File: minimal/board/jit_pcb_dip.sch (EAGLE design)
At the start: 44 parts, among them Q2 MC-306 32.7680K-A0, U1 FT232RL

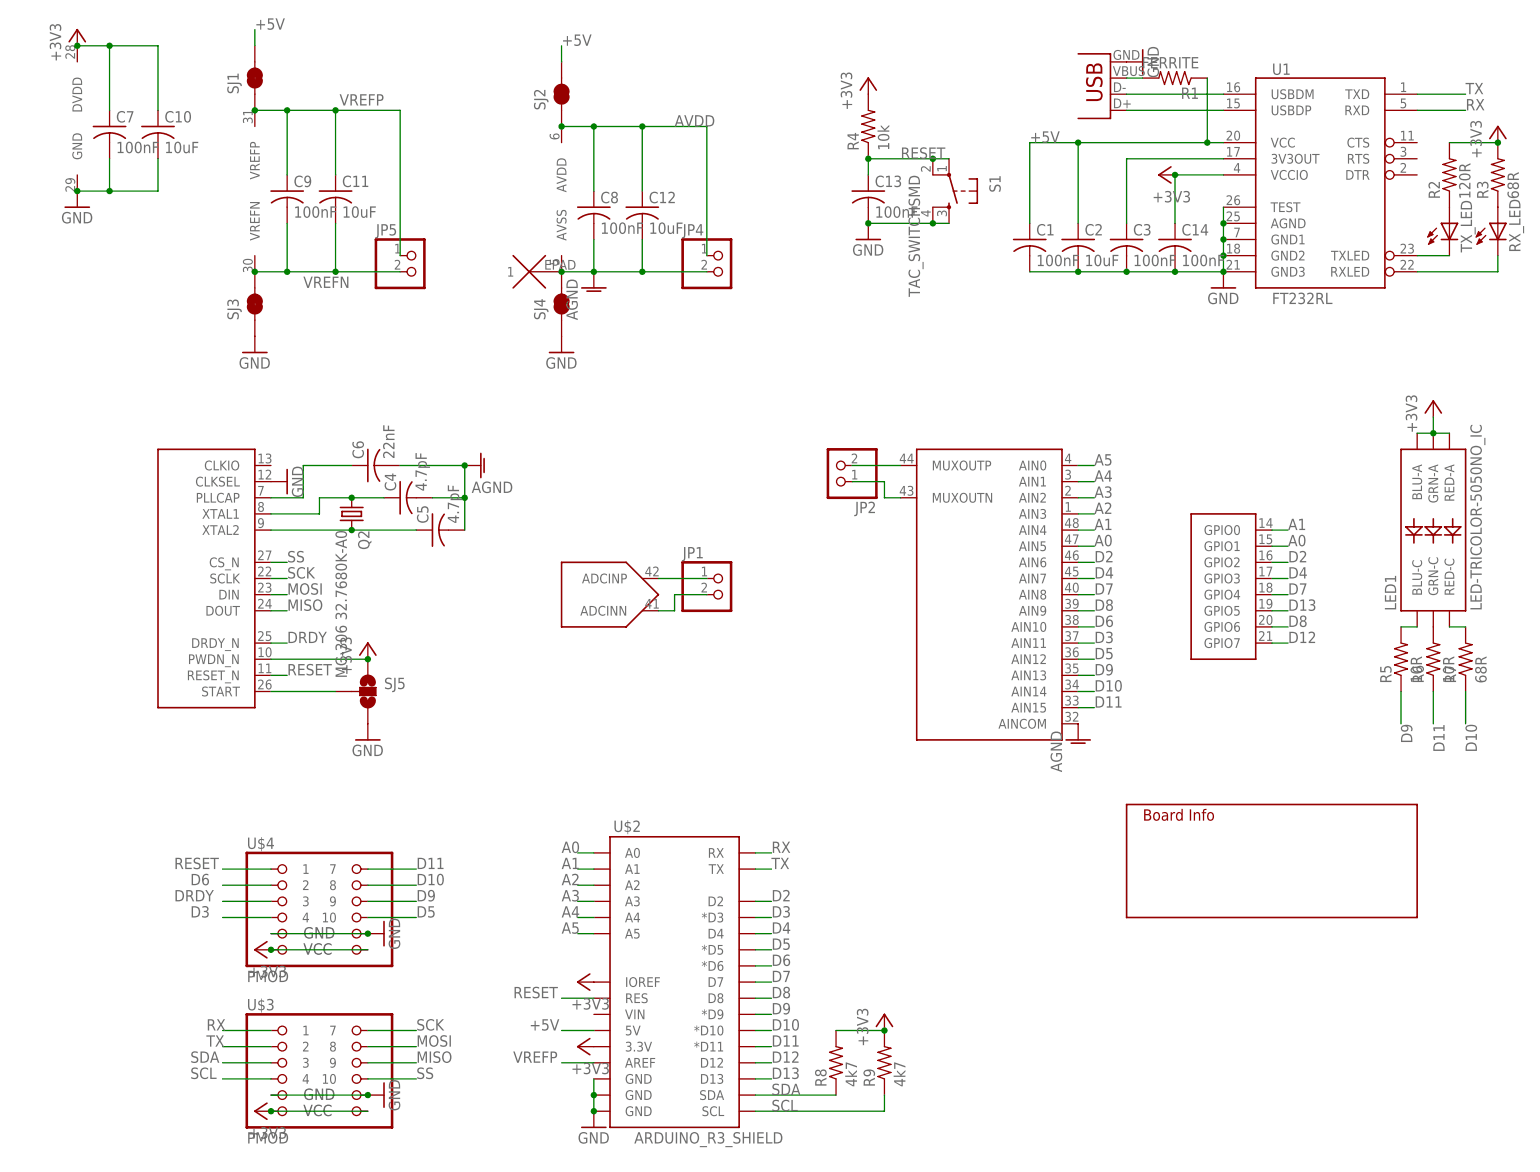
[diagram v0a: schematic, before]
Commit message: Adding all boards for minimal and carrier board with MKL05Z32
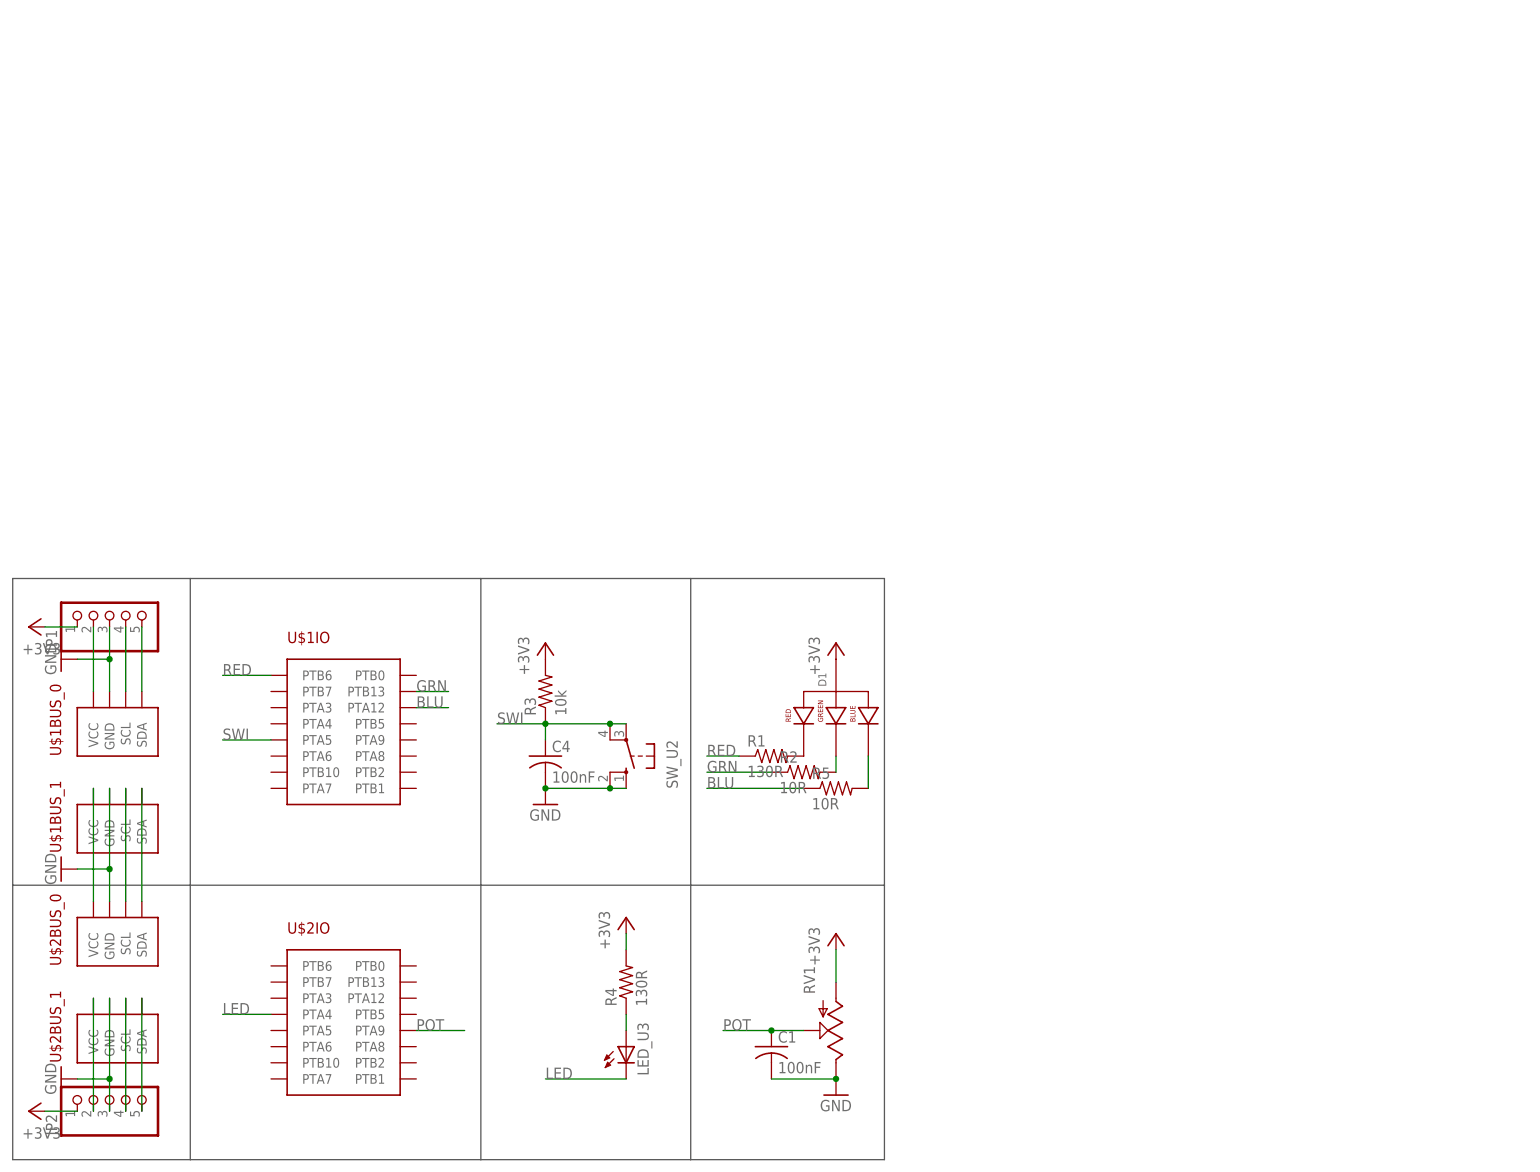
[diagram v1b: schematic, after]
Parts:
- removed C10, C11, C12, C2: 10uF, rcl:C-USC0603
- removed C13, C14, C3, C7, C8, C9: 100nF, rcl:C-USC0603
- removed C5: 4.7pF, rcl:C-USC0603
- removed C6: 22nF, rcl:C-USC0603
- removed JP3: USBSMD, SparkFun-Connectors:USBSMD
- removed JP4, JP5: (no value), pinhead:PINHD-1X2
- removed LED1: LED-TRICOLOR-5050NO_IC, SparkFun-LED:LED-TRICOLOR-5050NO_IC
- removed Q2: MC-306 32.7680K-A0, crystal:MC-306
- removed R6: 10R, rcl:R-US_R0603
- removed R7: 68R, rcl:R-US_R0603
- removed R8, R9: 4k7, rcl:R-US_R0603
- removed RX_LED, TX_LED: (no value), led:LEDCHIPLED_0603
- removed S1: TAC_SWITCHSMD, SparkFun-Electromechanical:TAC_SWITCHSMD
- removed SJ1, SJ2, SJ3, SJ4: JUMPER-PAD-2-NC_BY_TRACE, SparkFun-Passives:JUMPER-PAD-2-NC_BY_TRACE
- removed SJ5: JUMPER-PAD-3-NOYES_SILK, SparkFun-Passives:JUMPER-PAD-3-NOYES_SILK
- removed U$3, U$4: PMOD, modular_robotics:PMOD
- removed U$5: INFO, modular_robotics:INFO
- removed U1: FT232RL, SparkFun-DigitalIC:FT232RL-BASICSSOP
- added D1: LED-RGB-CA-THRUDIFFUSE, modular_robotics:LED-RGB-CA-THRUDIFFUSE
- added LED_U3: (no value), led:LED5MM
- added RV1: (no value), SparkFun-Electromechanical:POT100K_3362U
- added SW_U2: (no value), switch-omron:10-XX
- C1: device rcl:C-USC0603 -> rcl:C-US025-025X050
- C4: value 4.7pF -> 100nF; device rcl:C-USC0603 -> rcl:C-US025-025X050
- JP1, JP2: device pinhead:PINHD-1X2 -> pinhead:PINHD-1X5
- R1: value FERRITE -> 130R; device rcl:R-US_R0603 -> rcl:R-US_0204/7
- R2: value 120R -> 10R; device rcl:R-US_R0603 -> rcl:R-US_0204/7
- R3: value 68R -> 10k; device rcl:R-US_R0603 -> rcl:R-US_0204/7
- R4: value 10k -> 130R; device rcl:R-US_R0603 -> rcl:R-US_0204/7
- R5: device rcl:R-US_R0603 -> rcl:R-US_0204/7
- U$1: value ADS1258 -> MODROB_CARRIER-DIP; device modular_robotics:ADS1258 -> modular_robotics:MODROB_CARRIER-DIP
- U$2: value ARDUINO_R3_SHIELD -> MODROB_CARRIER-DIP; device SparkFun-Boards:ARDUINO_R3_SHIELD -> modular_robotics:MODROB_CARRIER-DIP
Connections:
- removed net +5V: C1.1, C2.1, R1.1, SJ1.2, SJ2.2, U$2.5V, U1.VCC
- removed net A0: U$1GPIO.GPIO1, U$1MUX.AIN5, U$2.A0
- removed net A1: U$1GPIO.GPIO0, U$1MUX.AIN4, U$2.A1
- removed net A2: U$1MUX.AIN3, U$2.A2
- removed net A3: U$1MUX.AIN2, U$2.A3
- removed net A4: U$1MUX.AIN1, U$2.A4
- removed net A5: U$1MUX.AIN0, U$2.A5
- removed net ADCN: JP1.2, U$1ADC.ADCINN
- removed net ADCP: JP1.1, U$1ADC.ADCINP
- removed net AGND: C12.2, C4.2, C5.2, C6.2, C8.2, JP4.2, SJ4.2, U$1AVDD-AVSS.AVSS, U$1EPAD.1, U$1MUX.AINCOM
- removed net AVDD: C12.1, C8.1, JP4.1, SJ2.1, U$1AVDD-AVSS.AVDD
- removed net D10: R7.1, U$1MUX.AIN14, U$2.*D10, U$4.8
- removed net D11: R6.1, U$1MUX.AIN15, U$2.*D11, U$4.7
- removed net D12: U$1GPIO.GPIO7, U$2.D12
- removed net D13: U$1GPIO.GPIO5, U$2.D13
- removed net D2: U$1GPIO.GPIO2, U$1MUX.AIN6, U$2.D2
- removed net D3: U$1MUX.AIN11, U$2.*D3, U$4.4
- removed net D4: U$1GPIO.GPIO3, U$1MUX.AIN7, U$2.D4
- removed net D5: U$1MUX.AIN12, U$2.*D5, U$4.10
- removed net D6: U$1MUX.AIN10, U$2.*D6, U$4.2
- removed net D7: U$1GPIO.GPIO4, U$1MUX.AIN8, U$2.D7
- removed net D8: U$1GPIO.GPIO6, U$1MUX.AIN9, U$2.D8
- removed net D9: R5.1, U$1MUX.AIN13, U$2.*D9, U$4.9
- removed net DRDY: U$1CTRL.DRDY_N, U$4.3
- removed net MISO: U$1CTRL.DOUT, U$3.9
- removed net MOSI: U$1CTRL.DIN, U$3.8
- removed net MUXN: JP2.1, U$1MUX.MUXOUTN
- removed net MUXP: JP2.2, U$1MUX.MUXOUTP
- removed net N$17: LED1.BLU-C, R5.2
- removed net N$18: LED1.GRN-C, R6.2
- removed net N$21: LED1.RED-C, R7.2
- removed net RESET: C13.1, R4.1, S1.1, S1.2, U$1CTRL.RESET_N, U$2.RES, U$4.1
- removed net RX: U$2.RX, U$3.1, U1.RXD
- removed net SCK: U$1CTRL.SCLK, U$3.7
- removed net SCL: R9.1, U$2.SCL, U$3.4
- removed net SDA: R8.1, U$2.SDA, U$3.3
- removed net SS: U$1CTRL.CS_N, U$3.10
- removed net TX: U$2.TX, U$3.2, U1.TXD
- removed net VREFN: C11.2, C9.2, JP5.2, SJ3.2, U$1VREFN-VREFP.VREFN
- removed net VREFP: C11.1, C9.1, JP5.1, SJ1.1, U$1VREFN-VREFP.VREFP, U$2.AREF
- new net BLU: R5.1, U$1IO.PTA12
- new net GRN: R2.1, U$1IO.PTB13
- new net LED: LED_U3.C, U$2IO.PTA4
- new net N$10: JP2.5, U$2BUS_1.SDA
- new net POT: C1.1, RV1.S, U$2IO.PTA9
- new net RED: R1.1, U$1IO.PTB6
- new net SWI: C4.1, R3.1, SW_U2.P, SW_U2.P1, U$1IO.PTA5
- net +3V3: now also D1.ANODE, JP1.1, JP2.1, RV1.A; no longer C10.1, C14.1, C7.1, LED1.BLU-A, LED1.GRN-A, LED1.RED-A, R2.2, R8.2, R9.2, SJ5.1, U$1CTRL.PWDN_N, U$1GND-DVDD.DVDD, U$2.3.3V, U$2.IOREF, U$3.12, U$3.6, U$4.12, U$4.6, U1.VCCIO
- net GND: now also C4.2, JP1.3, JP2.3, RV1.E, SW_U2.S, SW_U2.S1, U$1BUS_0.GND, U$1BUS_1.GND, U$2BUS_0.GND, U$2BUS_1.GND; no longer C10.2, C13.2, C14.2, C2.2, C3.2, C7.2, JP3.GND, S1.3, S1.4, SJ3.1, SJ4.1, SJ5.3, U$1CTRL.CLKSEL, U$1GND-DVDD.GND, U$2.GND@0, U$2.GND@1, U$2.GND@2, U$3.11, U$3.5, U$4.11, U$4.5, U1.AGND, U1.GND1, U1.GND2, U1.GND3, U1.TEST
- net N$1: now also JP1.2, U$1BUS_0.VCC; no longer JP3.D+, U1.USBDP
- net N$13: now also D1.RED_CATHODE, R1.2; no longer C6.1, U$1CTRL.PLLCAP
- net N$14: now also D1.GREEN_CATHODE, R2.2; no longer C4.1, Q2.1, U$1CTRL.XTAL1
- net N$15: now also D1.BLUE_CATHODE, R5.2; no longer C5.1, Q2.2, U$1CTRL.XTAL2
- net N$2: now also U$1BUS_1.VCC, U$2BUS_0.VCC; no longer JP3.D-, U1.USBDM
- net N$3: now also JP1.4, U$1BUS_0.SCL; no longer R2.1, TX_LED.A
- net N$4: now also LED_U3.A, R4.1; no longer R3.1, RX_LED.A
- net N$5: now also JP1.5, U$1BUS_0.SDA; no longer C3.1, U1.3V3OUT
- net N$6: now also JP2.2, U$2BUS_1.VCC; no longer SJ5.2, U$1CTRL.START
- net N$7: now also U$1BUS_1.SCL, U$2BUS_0.SCL; no longer JP3.VBUS, R1.2
- net N$8: now also U$1BUS_1.SDA, U$2BUS_0.SDA; no longer TX_LED.C, U1.TXLED
- net N$9: now also JP2.4, U$2BUS_1.SCL; no longer RX_LED.C, U1.RXLED
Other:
- moved on the sheet: C1, C4, R1, R2, R3, R4, R5
